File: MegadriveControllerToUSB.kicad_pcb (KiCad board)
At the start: 2 copper layers, 39.6 x 45.3 mm, 13 parts, among them CON1 AVR-ISP6, J1 USB, J2 DB9, U1 ATMEGA32U2-AU, X1 16Mhz

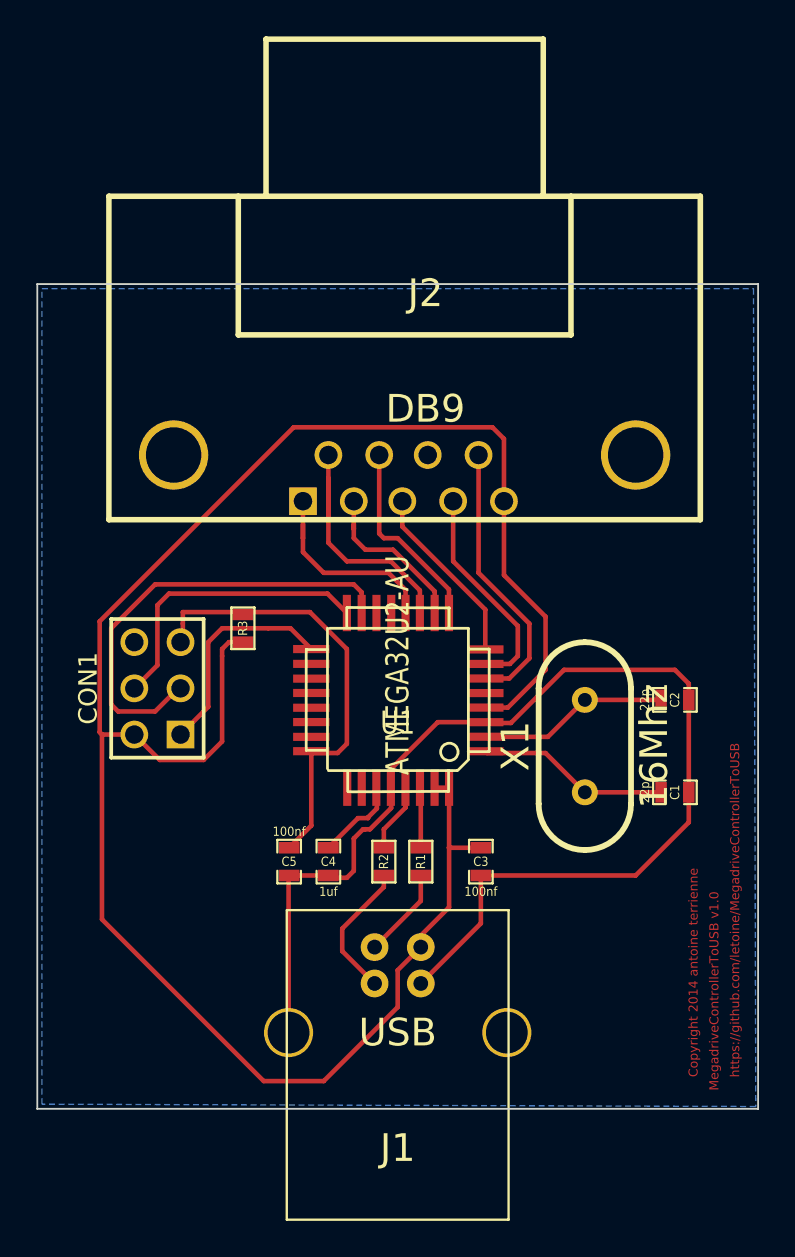
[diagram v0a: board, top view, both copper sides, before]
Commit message: Shrink board.
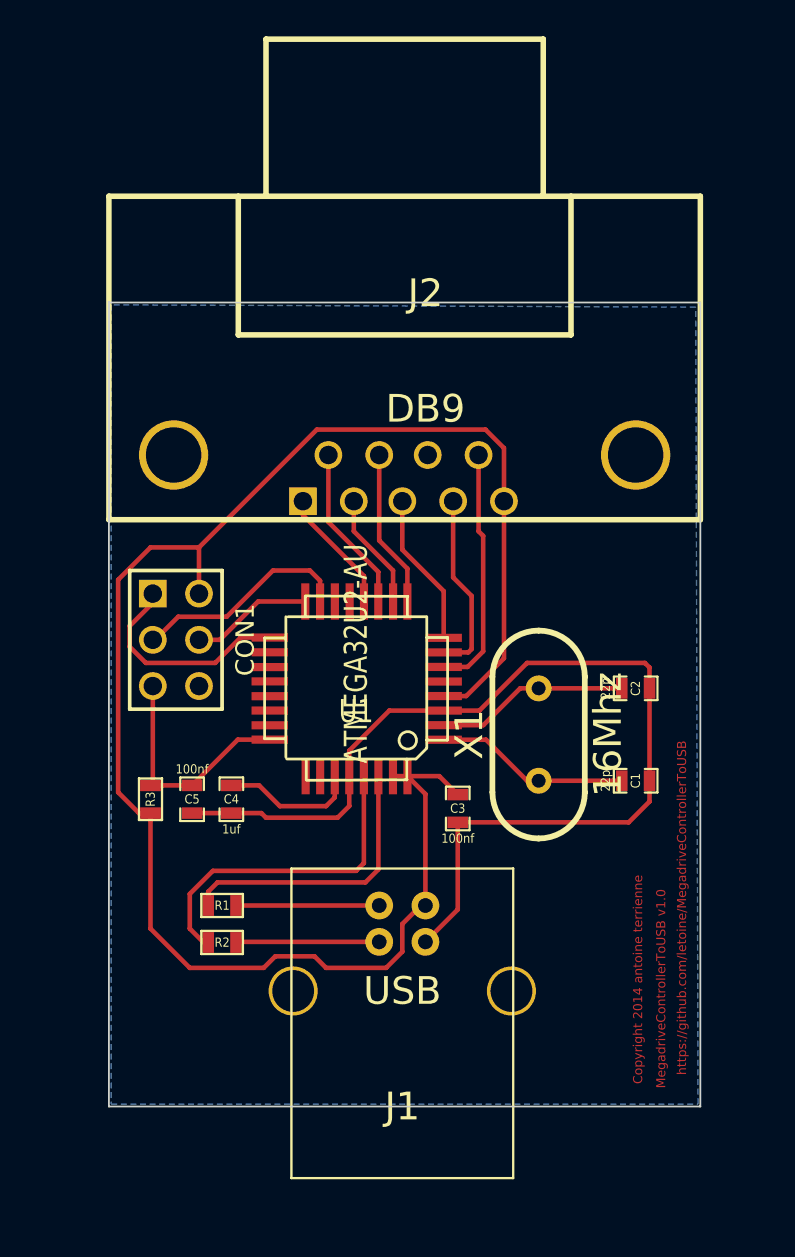
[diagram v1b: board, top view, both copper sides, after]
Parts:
- moved R1 11.2 mm to (200.9, 154.8), turned to 180 degrees
- moved R3 10.7 mm to (197.0, 149.0)
- moved R2 9.94 mm to (200.9, 156.8), turned to 180 degrees
- moved C4 6.34 mm to (201.4, 149.0)
- moved C5 6.34 mm to (199.3, 149.0)
- moved C3 3.19 mm to (213.9, 149.5)
- moved CON1 2.85 mm to (198.4, 140.2), turned to 270 degrees
- moved X1 2.62 mm to (218.3, 145.4)
- moved U1 2.37 mm to (208.3, 142.9)
- moved J1 2.30 mm to (210.8, 159.5)
- moved C1 2.25 mm to (223.6, 148.0)
- moved C2 2.25 mm to (223.6, 142.9)
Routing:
- net VCC: track 112.7 -> 94.0 mm
- net N-0000029: track 3.79 -> 18.3 mm
- net SCK: track 24.8 -> 12.1 mm
- net N-000004: track 3.32 -> 15.7 mm
- net RESET: track 24.9 -> 13.1 mm
- net MOSI: track 16.2 -> 6.72 mm
- net GND: track 65.6 -> 56.4 mm
- net C_START_BUTTON: track 14.2 -> 9.19 mm
- net UP_Z: track 11.3 -> 6.90 mm
- net N-000005: track 4.99 -> 7.87 mm
- net N-000003: track 4.74 -> 7.53 mm
- net DOWN_Y: track 9.13 -> 6.41 mm
- net SELECT_CLK: track 10.7 -> 8.69 mm
- net B_A_BUTTON: track 15.2 -> 13.4 mm
- net RIGHT_MODE: track 12.0 -> 10.2 mm
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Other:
- board size 39.6 x 45.3 mm -> 32.5 x 44.2 mm
